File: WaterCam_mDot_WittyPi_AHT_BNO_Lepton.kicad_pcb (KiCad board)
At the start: 2 copper layers, 116.3 x 65.3 mm, 8 parts, among them J1 GPIO, J2 FLIR Lepton Socket, J3 Witty Pi 4 L3V7 P3 Header, Q1 NMOS, U1 ATH20, U2 BNO055(IMU), U3 MDOT

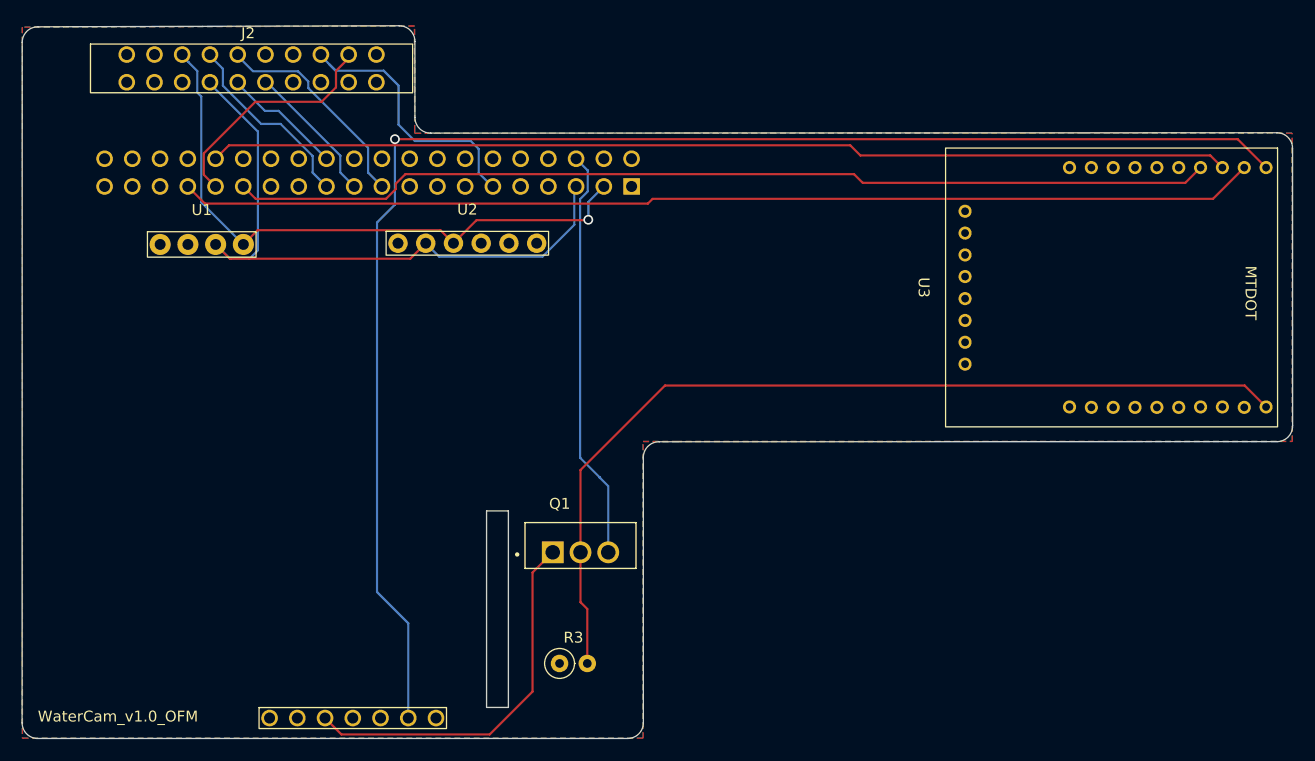
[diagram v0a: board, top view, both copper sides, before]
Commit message: Refine PCB power and ground layout for improved integrity and manufacturability
- Localized 5V plane to FLIR and IMU region to reduce EMI and isolate power
- Maintained full-board GND plane on bottom layer for low-impedance return paths
- Verified through-hole pad connections to both copper layers
- Removed unnecessary global power fills to prevent noise injection
- Cleaned up trace routing and ensured adequate spacing from board edges
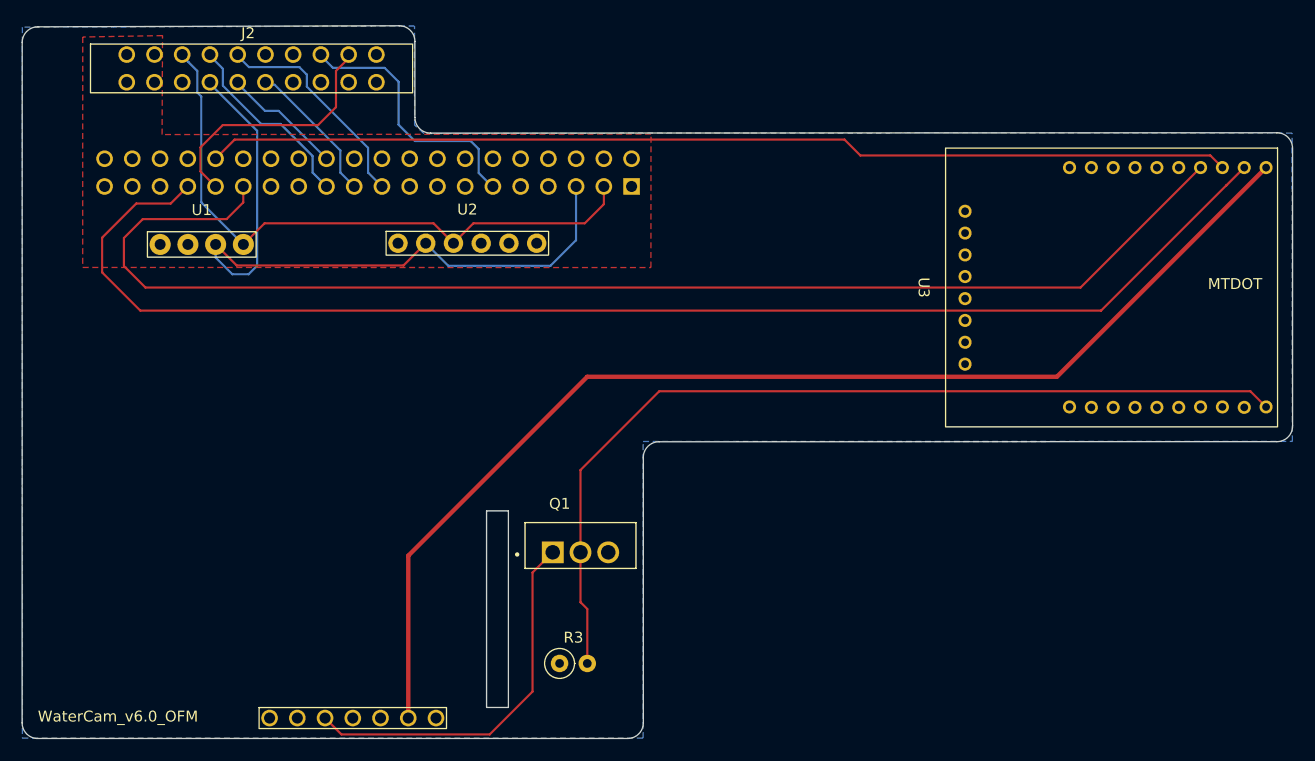
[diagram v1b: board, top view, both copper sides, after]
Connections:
- J3 pad 7: unconnected-(J3-GND-Pad7) -> GND
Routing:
- net GND: track 37.9 -> 0.00 mm
- net /GPIO5: track 90.3 -> 120.3 mm
- net Net-(J3-3V3): track 135.7 -> 108.1 mm, vias 1 -> 0
- net /GPIO13/PWM1: track 98.8 -> 125.0 mm
- net /GPIO3/SCL1: track 60.9 -> 65.7 mm
- net /GPIO6: track 21.4 -> 23.2 mm
- net /GPIO17: track 25.5 -> 24.8 mm
- net /GPIO2/SDA1: track 56.6 -> 57.1 mm, vias 1 -> 0
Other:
- board text added: "WaterCam_v6.0_OFM"
- board text removed: "WaterCam_v1.0_OFM"

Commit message: Refactor silkscreen, component labels, and routing to align with Raspberry Pi and improve power integrity
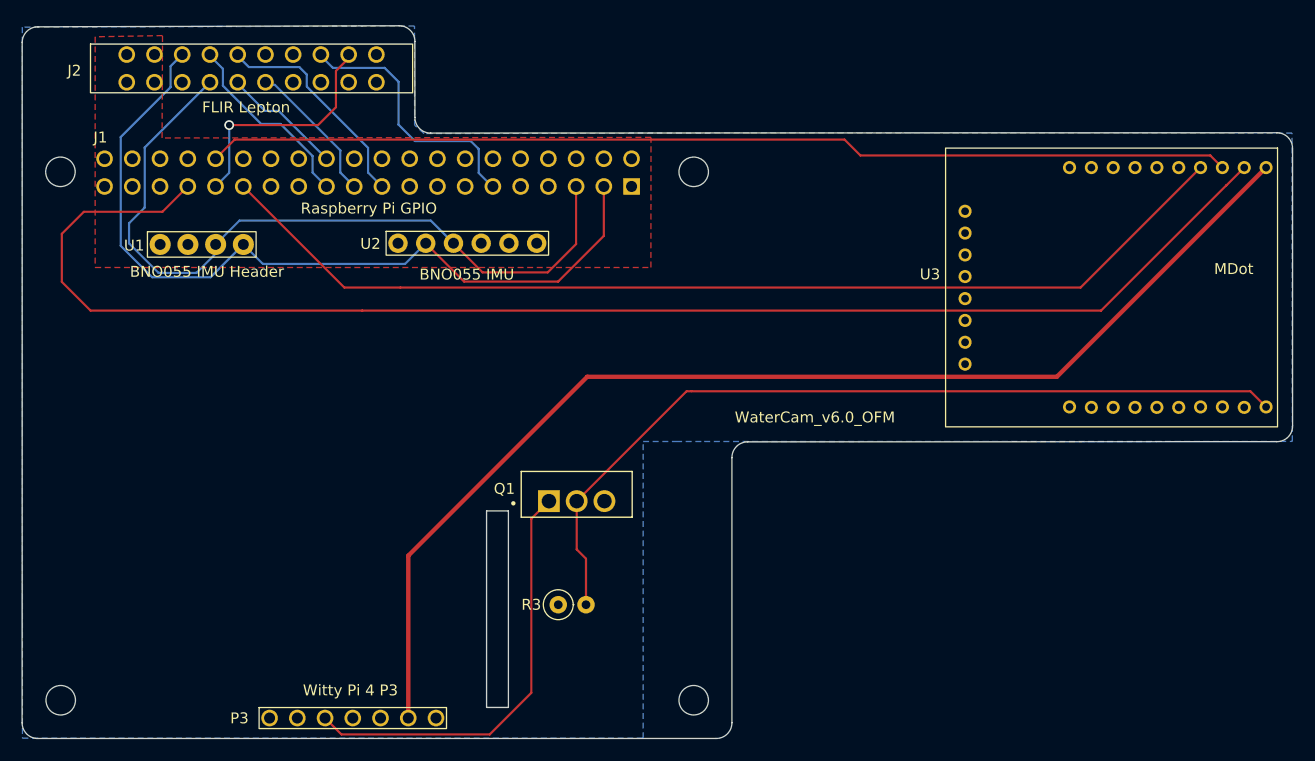
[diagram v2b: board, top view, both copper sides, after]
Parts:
- added REF**: MountingHole_2.7mm_M2.5, MountingHole:MountingHole_2.7mm_M2.5, F.Cu at (56.0, 96.4)
- added REF**: MountingHole_2.7mm_M2.5, MountingHole:MountingHole_2.7mm_M2.5, F.Cu at (113.9, 96.4)
- added REF**: MountingHole_2.7mm_M2.5, MountingHole:MountingHole_2.7mm_M2.5, F.Cu at (56.0, 48.0)
- added REF**: MountingHole_2.7mm_M2.5, MountingHole:MountingHole_2.7mm_M2.5, F.Cu at (113.9, 48.0)
- J2: value FLIR Lepton Socket -> FLIR Lepton
- P3: renamed from J3; value Witty Pi 4 L3V7 P3 Header -> Witty Pi 4 P3
- U2: value BNO055(IMU) -> BNO055 IMU
- moved R3 5.38 mm to (101.5, 87.6)
- moved Q1 4.70 mm to (103.2, 78.1)
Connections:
- U2 pad 2: /GPIO3/SCL1 -> /GPIO2/SDA1
- U2 pad 3: /GPIO2/SDA1 -> /GPIO3/SCL1
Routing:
- net /GPIO5: track 120.3 -> 96.0 mm
- net /GPIO2/SDA1: track 57.1 -> 75.8 mm
- net /GPIO13/PWM1: track 125.0 -> 133.1 mm
- net Net-(Q1-G): track 84.3 -> 78.6 mm
- net /GPIO3/SCL1: track 65.7 -> 70.7 mm
- net Net-(J3-SW): track 34.8 -> 39.3 mm
- net /GPIO6: track 23.2 -> 21.7 mm, vias 0 -> 1
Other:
- outline, holes or cut-outs redrawn
- board text added: "BNO055 IMU Header"
- board text added: "Raspberry Pi GPIO"
